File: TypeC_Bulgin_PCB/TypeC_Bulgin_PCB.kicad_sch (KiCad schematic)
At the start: 4 parts, among them J1 Conn_01x01_Female, J3 Conn_01x13, J4 Conn_01x13, J6 USB_C_Receptacle

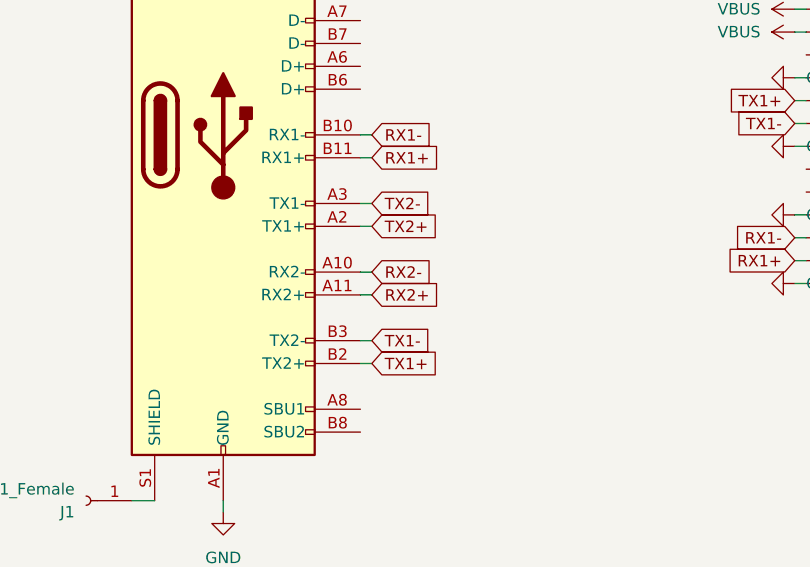
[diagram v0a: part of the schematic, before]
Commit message: v0.2 TXn were swapped
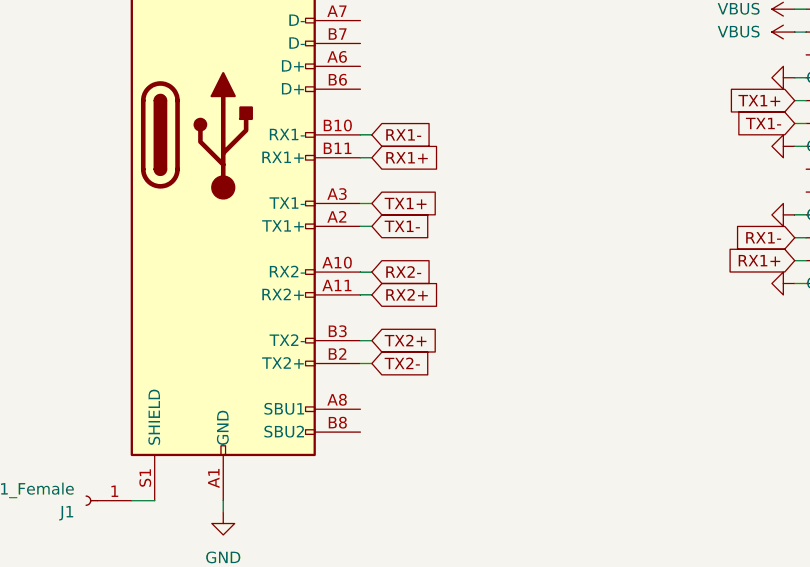
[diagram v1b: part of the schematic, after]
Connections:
- net TX1+: now also J6.A3 (TX1-); no longer J6.B2 (TX2+)
- net TX1-: now also J6.A2 (TX1+); no longer J6.B3 (TX2-)
- net TX2+: now also J6.B3 (TX2-); no longer J6.A2 (TX1+)
- net TX2-: now also J6.B2 (TX2+); no longer J6.A3 (TX1-)
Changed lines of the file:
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@@
     (stroke (width 0) (type default) (color 0 0 0 0))
   )
-  (wire (pts (xy 143.51 102.87) (xy 144.78 102.87))
+  (wire (pts (xy 144.78 87.63) (xy 143.51 87.63))
     (stroke (width 0) (type default) (color 0 0 0 0))
   )
@@
     (stroke (width 0) (type default) (color 0 0 0 0))
   )
+  (wire (pts (xy 144.78 85.09) (xy 143.51 85.09))
+    (stroke (width 0) (type default) (color 0 0 0 0))
+  )
   (wire (pts (xy 191.77 91.44) (xy 193.04 91.44))
+    (stroke (width 0) (type default) (color 0 0 0 0))
+  )
+  (wire (pts (xy 144.78 102.87) (xy 143.51 102.87))
     (stroke (width 0) (type default) (color 0 0 0 0))
   )
@@
   )
   (wire (pts (xy 143.51 80.01) (xy 144.78 80.01))
+    (stroke (width 0) (type default) (color 0 0 0 0))
+  )
+  (wire (pts (xy 144.78 100.33) (xy 143.51 100.33))
     (stroke (width 0) (type default) (color 0 0 0 0))
   )
@@
     (stroke (width 0) (type default) (color 0 0 0 0))
   )
-  (wire (pts (xy 143.51 87.63) (xy 144.78 87.63))
-    (stroke (width 0) (type default) (color 0 0 0 0))
-  )
-  (wire (pts (xy 143.51 100.33) (xy 144.78 100.33))
-    (stroke (width 0) (type default) (color 0 0 0 0))
-  )
   (wire (pts (xy 191.77 78.74) (xy 193.04 78.74))
     (stroke (width 0) (type default) (color 0 0 0 0))
@@
   )
   (wire (pts (xy 226.06 63.5) (xy 227.33 63.5))
-    (stroke (width 0) (type default) (color 0 0 0 0))
-  )
-  (wire (pts (xy 143.51 85.09) (xy 144.78 85.09))
     (stroke (width 0) (type default) (color 0 0 0 0))
   )
@@
     )
   )
-  (global_label "TX2-" (shape input) (at 144.78 85.09 0) (fields_autoplaced)
+  (global_label "TX2-" (shape input) (at 144.78 102.87 0) (fields_autoplaced)
     (effects (font (size 1.27 1.27)) (justify left))
-    (property "Intersheet References" "${INTERSHEET_REFS}" (id 0) (at 152.1521 85.0106 0)
+    (property "Intersheet References" "${INTERSHEET_REFS}" (id 0) (at 152.1521 102.7906 0)
       (effects (font (size 1.27 1.27)) (justify left) hide)
     )
@@
     )
   )
-  (global_label "TX1-" (shape input) (at 144.78 100.33 0) (fields_autoplaced)
+  (global_label "TX1-" (shape input) (at 144.78 87.63 0) (fields_autoplaced)
     (effects (font (size 1.27 1.27)) (justify left))
-    (property "Intersheet References" "${INTERSHEET_REFS}" (id 0) (at 152.1521 100.2506 0)
+    (property "Intersheet References" "${INTERSHEET_REFS}" (id 0) (at 152.1521 87.5506 0)
       (effects (font (size 1.27 1.27)) (justify left) hide)
     )
@@
     )
   )
-  (global_label "TX2+" (shape input) (at 144.78 87.63 0) (fields_autoplaced)
+  (global_label "TX2+" (shape input) (at 144.78 100.33 0) (fields_autoplaced)
     (effects (font (size 1.27 1.27)) (justify left))
-    (property "Intersheet References" "${INTERSHEET_REFS}" (id 0) (at 152.1521 87.5506 0)
+    (property "Intersheet References" "${INTERSHEET_REFS}" (id 0) (at 152.1521 100.2506 0)
       (effects (font (size 1.27 1.27)) (justify left) hide)
     )
@@
     )
   )
-  (global_label "TX1+" (shape input) (at 144.78 102.87 0) (fields_autoplaced)
+  (global_label "TX1+" (shape input) (at 144.78 85.09 0) (fields_autoplaced)
     (effects (font (size 1.27 1.27)) (justify left))
-    (property "Intersheet References" "${INTERSHEET_REFS}" (id 0) (at 152.1521 102.7906 0)
+    (property "Intersheet References" "${INTERSHEET_REFS}" (id 0) (at 152.1521 85.0106 0)
       (effects (font (size 1.27 1.27)) (justify left) hide)
     )

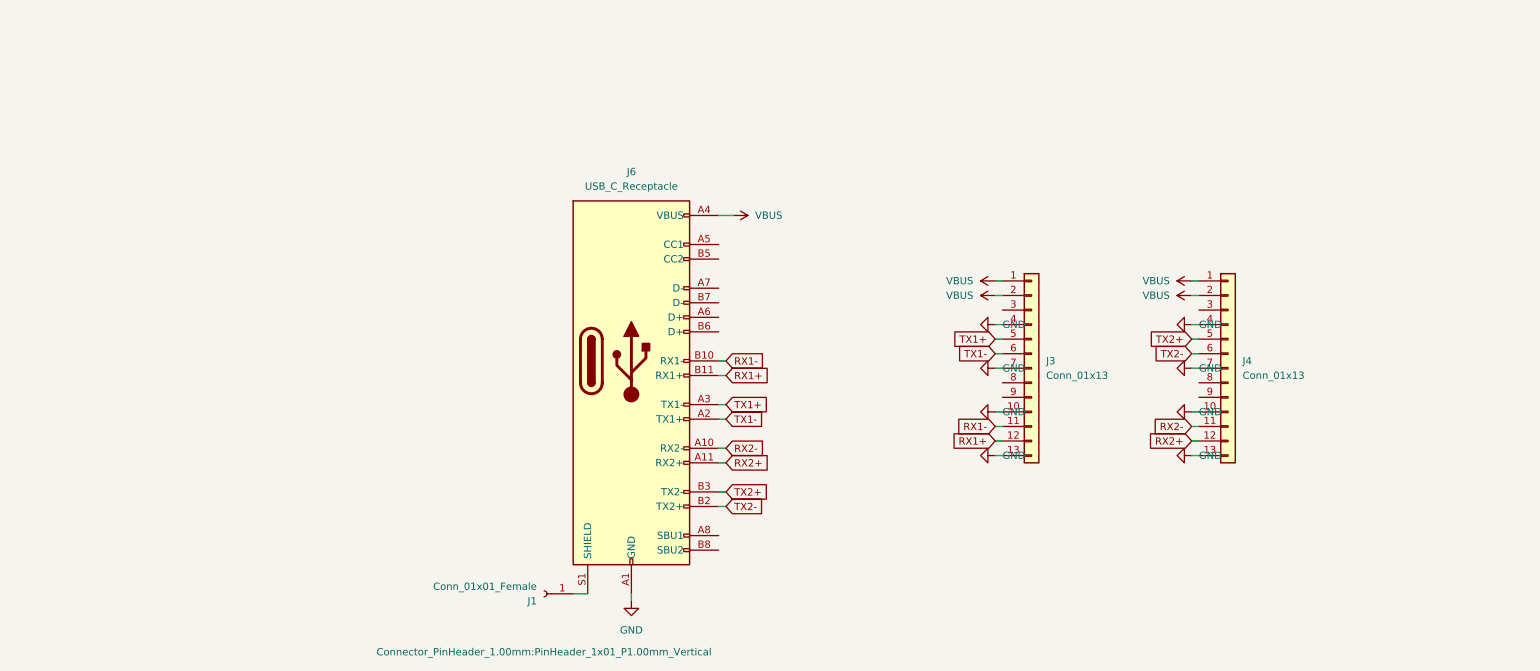
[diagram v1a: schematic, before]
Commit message: v0.64 USB circuit was added
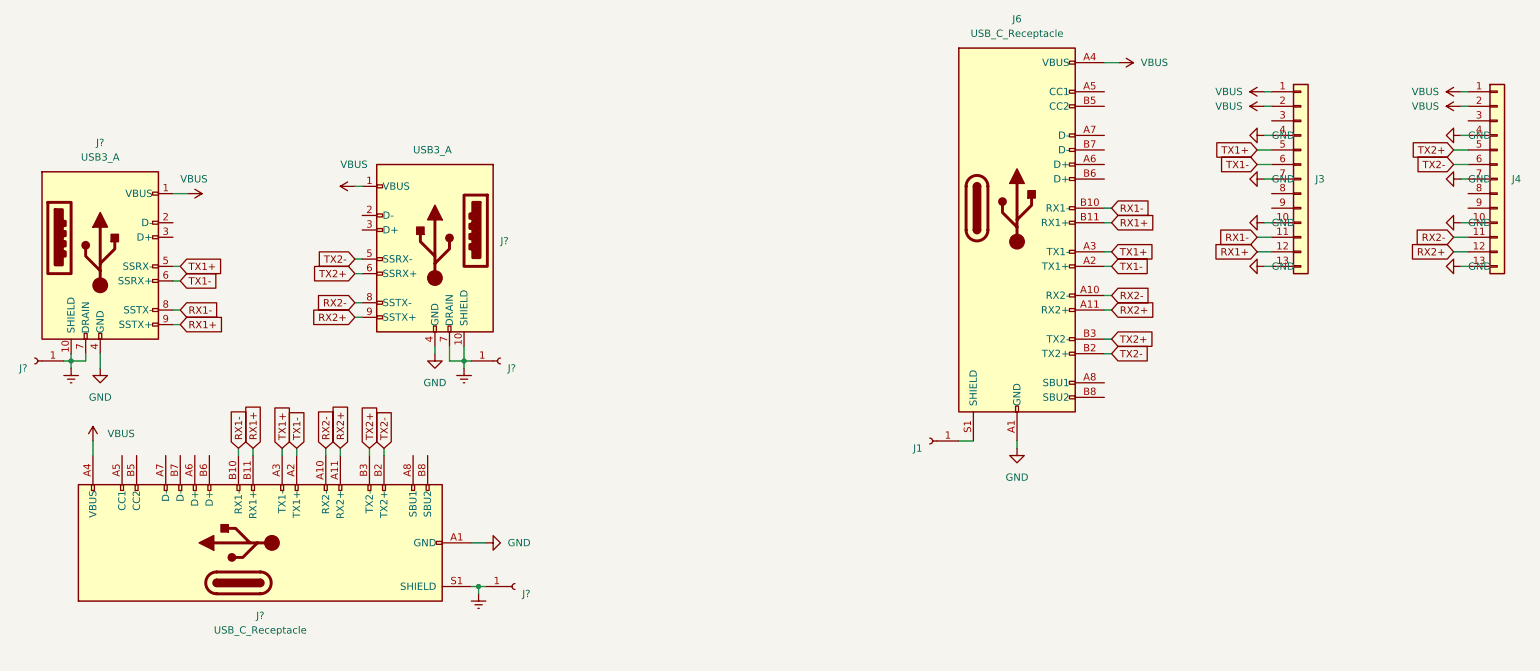
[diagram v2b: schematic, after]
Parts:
- added J?: USB_C_Receptacle, Connector_USB:USB_C_Receptacle_JAE_DX07S024WJ3R400, symbol TypeC_Bulgin_PCB:USB_C_Receptacle
- added J? (x3): Conn_01x01_Female, Connector_PinHeader_1.00mm:PinHeader_1x01_P1.00mm_Vertical, symbol Connector:Conn_01x01_Female
- added J? (x2): USB3_A, symbol Connector:USB3_A
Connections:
- net GND: now also J?.4 (GND), J?.4 (GND), J?.A1 (GND), J?.A12 (GND), J?.B1 (GND), J?.B12 (GND)
- net RX1+: now also J?.9 (SSTX+), J?.B11 (RX1+)
- net RX1-: now also J?.8 (SSTX-), J?.B10 (RX1-)
- net RX2+: now also J?.9 (SSTX+), J?.A11 (RX2+)
- net RX2-: now also J?.8 (SSTX-), J?.A10 (RX2-)
- net TX1+: now also J?.5 (SSRX-), J?.A3 (TX1-)
- net TX1-: now also J?.6 (SSRX+), J?.A2 (TX1+)
- net TX2+: now also J?.6 (SSRX+), J?.B3 (TX2-)
- net TX2-: now also J?.5 (SSRX-), J?.B2 (TX2+)
- net VBUS: now also J?.1 (VBUS), J?.1 (VBUS), J?.A4 (VBUS), J?.A9 (VBUS), J?.B4 (VBUS), J?.B9 (VBUS)
- new net Earth: J?.1 (Pin_1), J?.1 (Pin_1), J?.1 (Pin_1), J?.10 (SHIELD), J?.10 (SHIELD), J?.7 (DRAIN), J?.7 (DRAIN), J?.S1 (SHIELD)
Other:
- moved on the sheet: J1, J3, J4, J6
